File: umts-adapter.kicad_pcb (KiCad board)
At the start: 2 copper layers, 41.4 x 42.7 mm, 10 parts, among them J1 Conn_02x15_Counter_Clockwise, J2 DB9_Female_MountingHoles, J3 Conn_02x01, U1 L7805

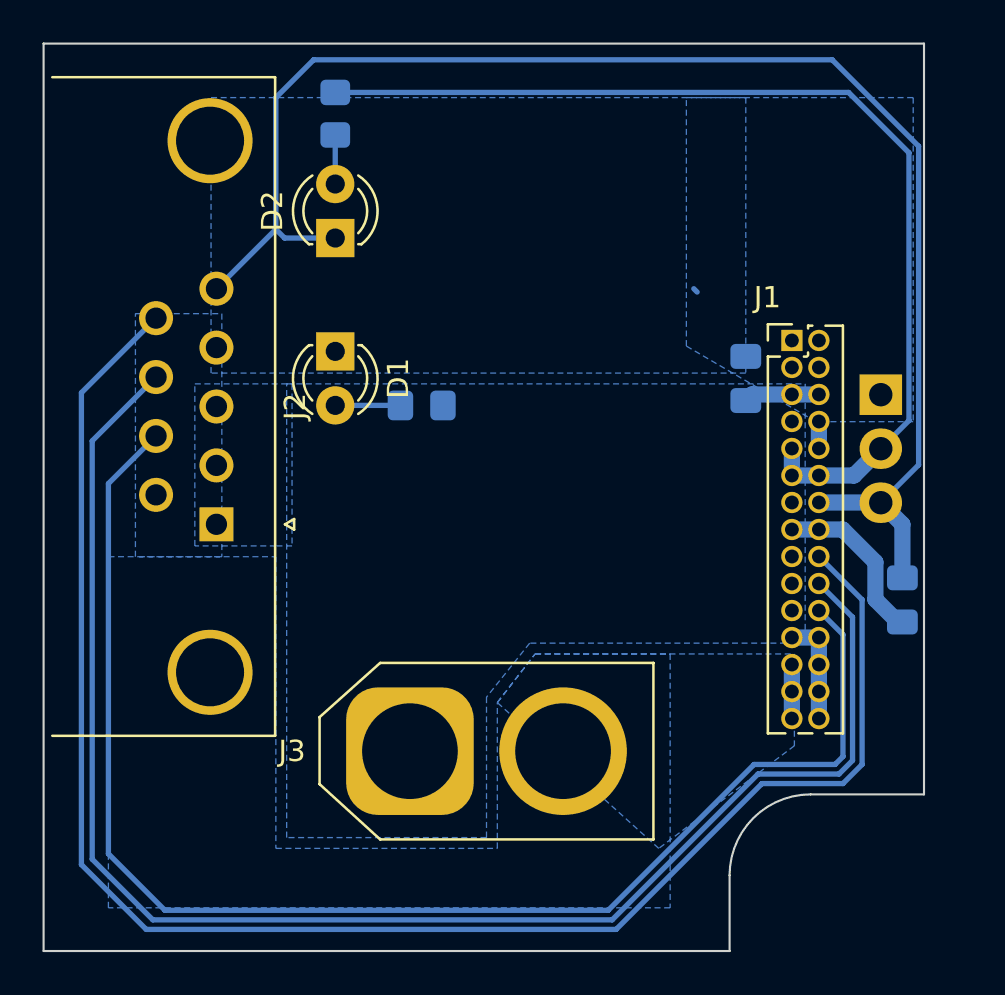
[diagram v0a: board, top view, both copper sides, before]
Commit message: feat: rev1.0, fits without cover. To be redesigned
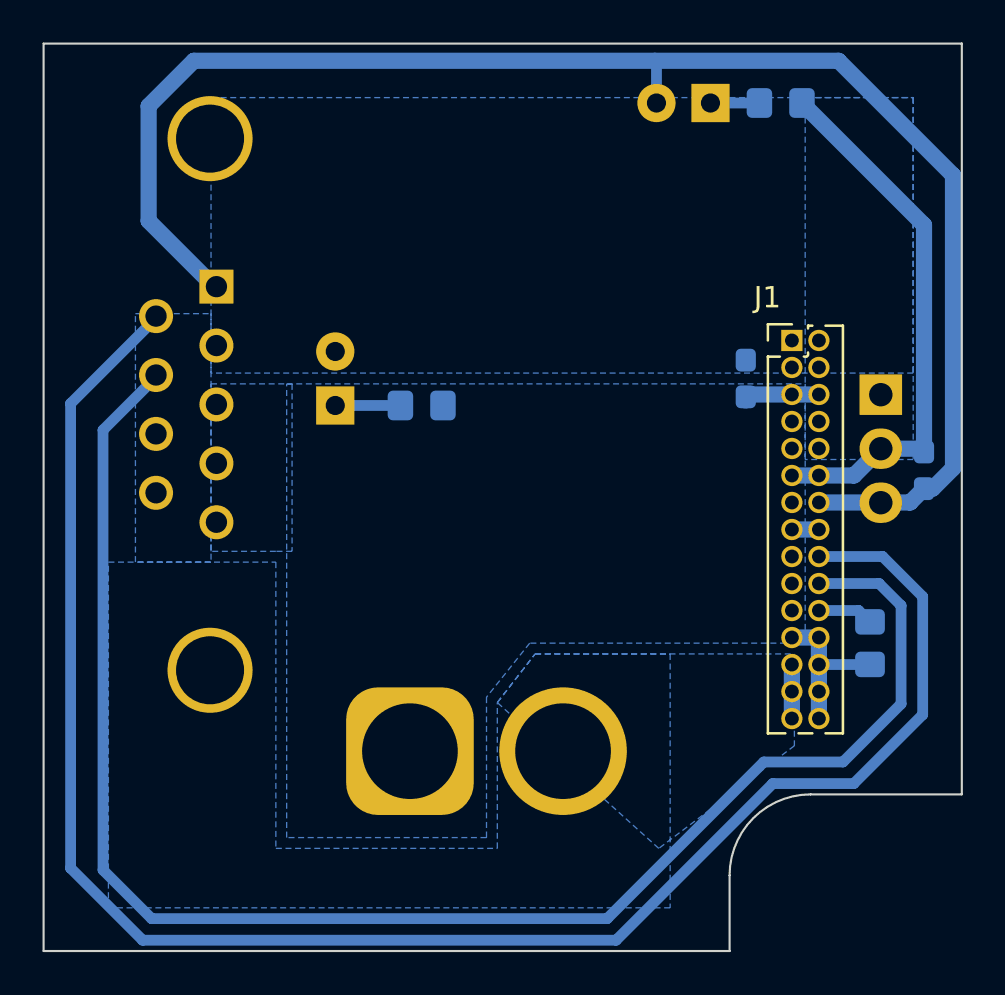
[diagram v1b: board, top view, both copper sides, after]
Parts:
- added R3: 5k, Resistor_SMD:R_0805_2012Metric_Pad1.20x1.40mm_HandSolder, B.Cu at (169.7, 56.1)
- C1, C2: footprint Capacitor_SMD:C_0805_2012Metric_Pad1.18x1.45mm_HandSolder -> Capacitor_SMD:C_0603_1608Metric_Pad1.08x0.95mm_HandSolder
- D1: value LED -> 28V OK; moved to B.Cu
- D2: value LED -> 5V OK; moved to B.Cu
- J1: value Conn_02x15_Counter_Clockwise -> UMTS POWER
- J2: value DB9_Female_MountingHoles -> DEBUG; moved to B.Cu
- J3: value Conn_02x01 -> POWER IN; moved to B.Cu
- moved R2 21.0 mm to (165.5, 30.7), turned to 0 degrees
- moved D2 18.8 mm to (162.2, 30.7), turned to 180 degrees
- moved J2 11.2 mm to (138.9, 39.4), turned to 90 degrees
- moved C2 6.18 mm to (172.2, 48.0), turned to 90 degrees
- moved D1 2.55 mm to (144.5, 45.0), turned to 90 degrees
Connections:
- D1 pad 1: +28V -> Net-(D1-Pad1)
- D1 pad 2: Net-(D1-Pad2) -> +28V
- D2 pad 1: +5V -> Net-(R2-Pad1)
- D2 pad 2: Net-(D2-Pad2) -> +5V
- J1 pad 22: /A0 -> Net-(J1-Pad22)
- J2 pad 1: GND -> +5V
- J2 pad 2: GND -> +28V
- J2 pad 4: +28V -> GND
- J2 pad 5: +5V -> GND
- J2 pad 6: /ptt -> /scl
- J2 pad 7: /A0 -> /sda
- J2 pad 8: /sda -> unconnected-(J2-Pad8)
- J2 pad 9: /scl -> /ptt
- R1 pad 1: Net-(D1-Pad2) -> Net-(D1-Pad1)
- R2 pad 1: Net-(D2-Pad2) -> Net-(R2-Pad1)
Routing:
- net /A0: track 66.6 -> 0.00 mm
- net GND: track 65.6 -> 37.9 mm
- net /scl: track 79.0 -> 84.6 mm
- net +5V: track 70.5 -> 73.6 mm
- net Net-(D1-Pad1): track 0.00 -> 3.06 mm
- net Net-(D1-Pad2): track 3.06 -> 0.00 mm
- net /sda: track 72.9 -> 75.8 mm
- net Net-(J1-Pad22): track 0.00 -> 2.62 mm
- net Net-(D2-Pad2): track 2.31 -> 0.00 mm
- net Net-(R2-Pad1): track 0.00 -> 2.30 mm
- net +28V: track 4.32 -> 2.54 mm
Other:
- board size 41.4 x 42.7 mm -> 43.2 x 42.7 mm

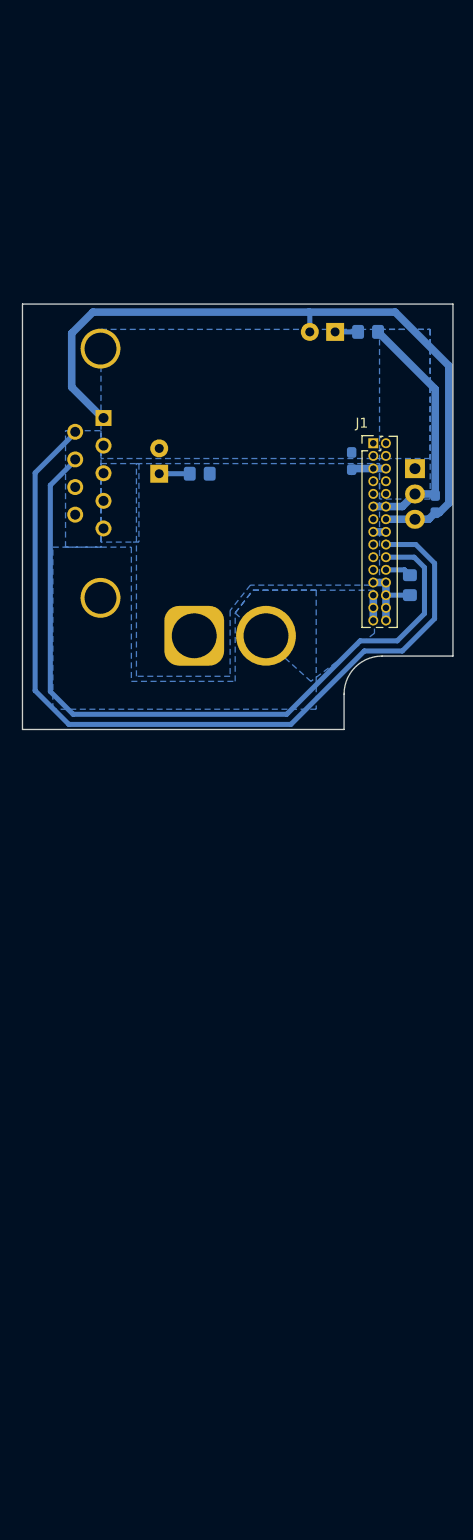
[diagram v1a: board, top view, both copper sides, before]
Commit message: !change: updated pcb to fit into built-in holes on the box change: two-stage adjustable regulators
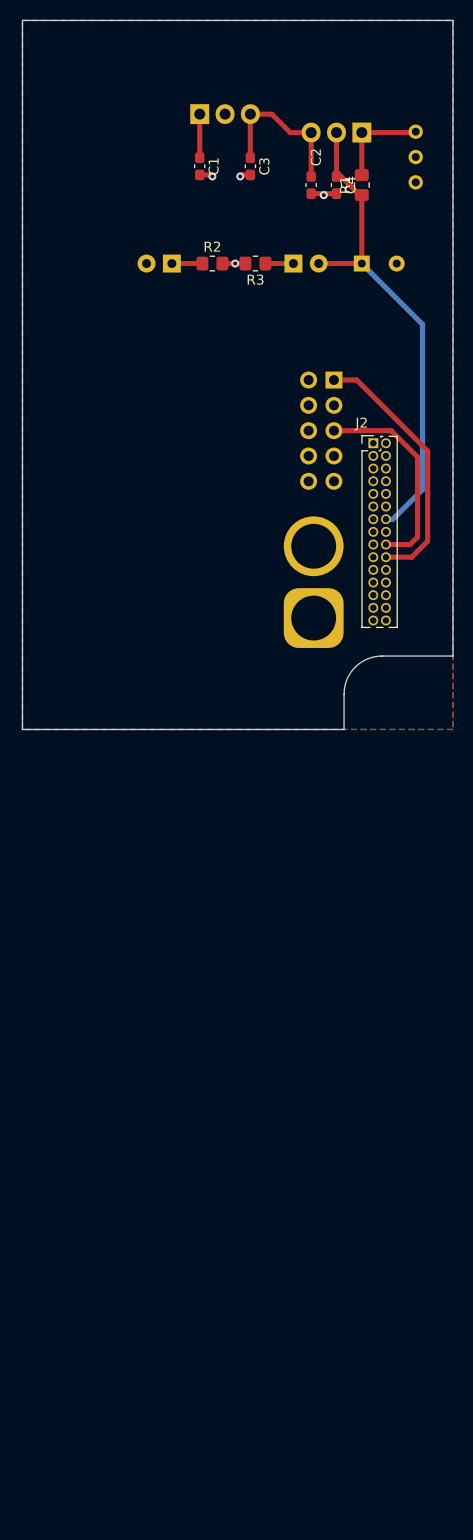
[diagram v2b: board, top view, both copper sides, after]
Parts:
- removed the J2 at (138.9, 39.4)
- removed the R3 at (169.7, 56.1)
- added C3: 0.1uF, Capacitor_SMD:C_0603_1608Metric_Pad1.08x0.95mm_HandSolder, F.Cu at (153.7, 14.1)
- added C4: 0.1uF, Capacitor_SMD:C_0603_1608Metric_Pad1.08x0.95mm_HandSolder, F.Cu at (162.3, 16.0)
- added C5: 100uF, Capacitor_THT:CP_Radial_D8.0mm_P3.50mm, B.Cu at (164.8, 23.9)
- added J3: Telemetry, Connector_PinHeader_2.54mm:PinHeader_2x05_P2.54mm_Vertical, B.Cu at (162.1, 35.6)
- added R1: 240, Resistor_SMD:R_0805_2012Metric_Pad1.20x1.40mm_HandSolder, F.Cu at (164.8, 16.0)
- added RV1: 2k, Potentiometer_THT:Potentiometer_Bourns_3266Y_Vertical, B.Cu at (170.3, 15.7)
- added U2: LM317_TO-220, Package_TO_SOT_THT:TO-220-3_Vertical, B.Cu at (164.8, 10.7)
- C1: value 0.22uF -> 0.33uF; moved to F.Cu
- C2: moved to F.Cu
- R2: renamed from R1; moved to F.Cu
- R3: renamed from R2; moved to F.Cu
- U1: value L7805 -> L7812
- moved U1 41.6 mm to (148.6, 8.89), turned to 0 degrees
- moved C2 34.3 mm to (159.8, 16.0), turned to -90 degrees
- moved C1 33.3 mm to (148.6, 14.1)
- moved R2 21.1 mm to (149.9, 23.9)
- moved D1 21.1 mm to (145.8, 23.9), turned to 180 degrees
- moved R3 13.2 mm to (154.2, 23.9), turned to 180 degrees
- moved J1 12.1 mm to (160.0, 59.4), turned to 90 degrees
- moved D2 8.03 mm to (158.0, 23.9), turned to 0 degrees
- renumbered J3 to J1, J1 to J2
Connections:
- C2 pad 1: +5V -> Net-(C2-Pad1)
- D2 pad 2: +5V -> VCC
- J2 pad 14: +5V -> VCC
- J2 pad 22: Net-(J1-Pad22) -> unconnected-(J2-Pad22)
- U1 pad 3: +5V -> Net-(C2-Pad1)
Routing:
- net +5V: track 73.6 -> 0.00 mm
- net /scl: track 84.6 -> 21.0 mm
- net /sda: track 75.8 -> 26.2 mm
- net VCC: track 0.00 -> 49.0 mm
- net GND: track 37.9 -> 7.40 mm, vias 0 -> 4
- net Net-(C2-Pad1): track 0.00 -> 15.6 mm
- net Net-(R1-Pad2): track 0.00 -> 9.71 mm
- net Net-(J1-Pad22): track 2.62 -> 0.00 mm
- net +28V: track 2.54 -> 4.37 mm
- net Net-(D2-Pad1): track 2.30 -> 2.81 mm
- added copper zone on F.Cu, net +28V
- removed copper zone on B.Cu, net +28V
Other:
- board size 43.2 x 42.7 mm -> 43.2 x 71.1 mm

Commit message: feat!: removed all extra components to make it just a breakout
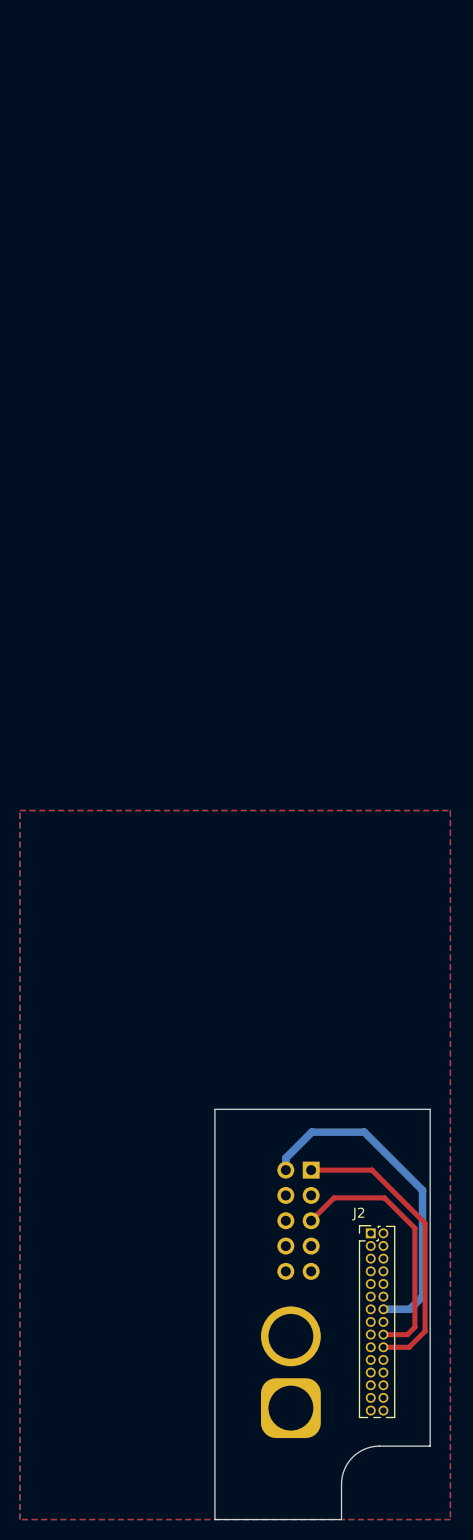
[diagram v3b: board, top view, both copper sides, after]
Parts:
- removed C1: 0.33uF, Capacitor_SMD:C_0603_1608Metric_Pad1.08x0.95mm_HandSolder
- removed C2, C3, C4: 0.1uF, Capacitor_SMD:C_0603_1608Metric_Pad1.08x0.95mm_HandSolder
- removed C5: 100uF, Capacitor_THT:CP_Radial_D8.0mm_P3.50mm
- removed D1: 28V OK, LED_THT:LED_D3.0mm
- removed D2: 5V OK, LED_THT:LED_D3.0mm
- removed R1: 240, Resistor_SMD:R_0805_2012Metric_Pad1.20x1.40mm_HandSolder
- removed R2: 27k, Resistor_SMD:R_0805_2012Metric_Pad1.20x1.40mm_HandSolder
- removed R3: 5k, Resistor_SMD:R_0805_2012Metric_Pad1.20x1.40mm_HandSolder
- removed RV1: 2k, Potentiometer_THT:Potentiometer_Bourns_3266Y_Vertical
- removed U1: L7812, Package_TO_SOT_THT:TO-220-3_Vertical
- removed U2: LM317_TO-220, Package_TO_SOT_THT:TO-220-3_Vertical
- moved J3 79.3 mm to (159.8, 114.8)
- moved J1 79.3 mm to (157.7, 138.7)
- moved J2 79.2 mm to (165.7, 121.1)
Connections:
- J3 pad 2: GND -> VCC
- J3 pad 6: +5V -> GND
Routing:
- net Net-(C2-Pad1): track 15.6 -> 0.00 mm
- net VCC: track 49.0 -> 33.5 mm
- net Net-(R1-Pad2): track 9.71 -> 0.00 mm
- net GND: track 7.40 -> 0.00 mm, vias 4 -> 0
- net /scl: track 21.0 -> 26.0 mm
- net +28V: track 4.37 -> 0.00 mm
- net /sda: track 26.2 -> 29.3 mm
- net Net-(D1-Pad1): track 3.06 -> 0.00 mm
- net Net-(D2-Pad1): track 2.81 -> 0.00 mm
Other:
- board size 43.2 x 71.1 mm -> 21.6 x 41.1 mm

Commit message: Update to fabricated & tested version
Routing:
- net /scl: track 26.0 -> 28.1 mm
- net /sda: track 29.3 -> 30.8 mm
- net VCC: track 33.5 -> 32.9 mm
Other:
- board size 21.6 x 41.1 mm -> 31.8 x 41.1 mm
